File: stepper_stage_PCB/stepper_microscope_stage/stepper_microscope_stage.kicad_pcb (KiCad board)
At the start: 2 copper layers, 160.5 x 149.2 mm, 27 parts, among them J1 Conn_01x04_Socket, J2 Screw_Terminal_01x04, J3 Screw_Terminal_01x04, J4 Conn_01x04_Socket, J5 Conn_01x04_Socket, SW1 SW_SPDT

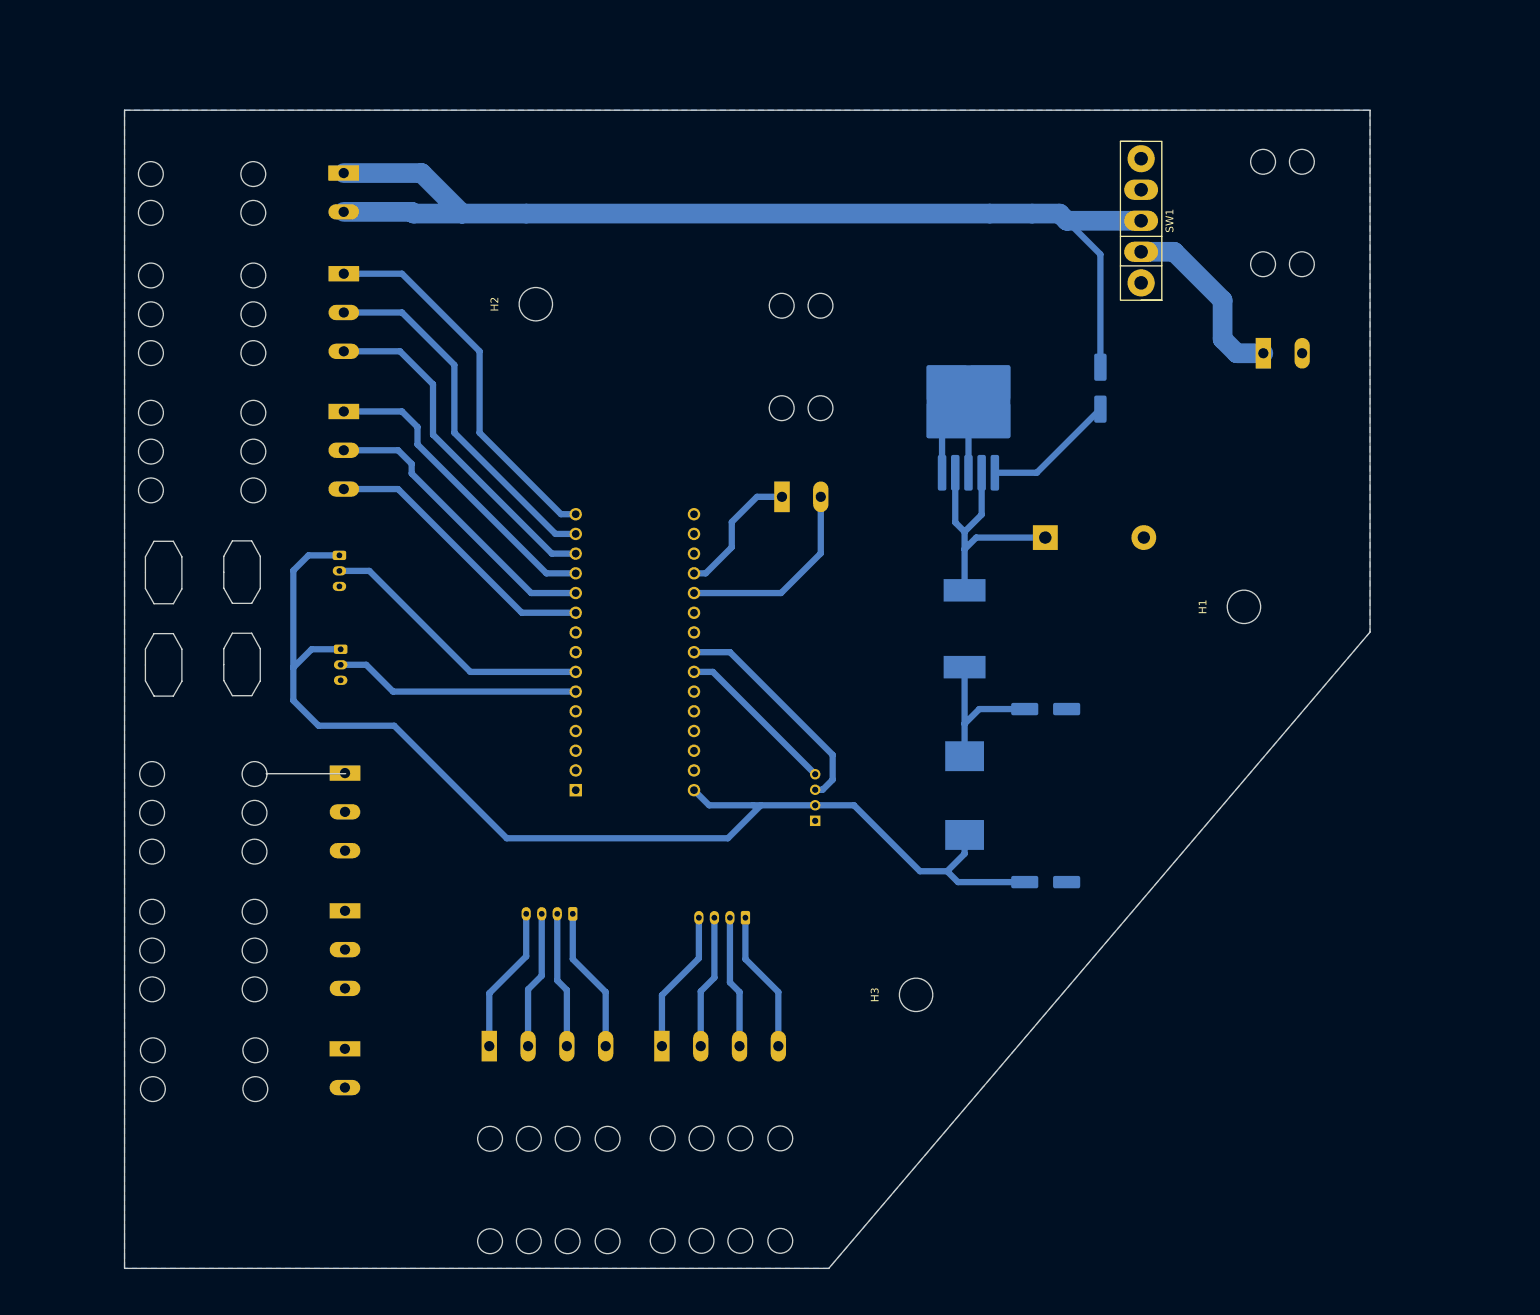
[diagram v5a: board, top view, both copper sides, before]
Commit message: Working. Must add following: (1) LCD space (2) ground plane
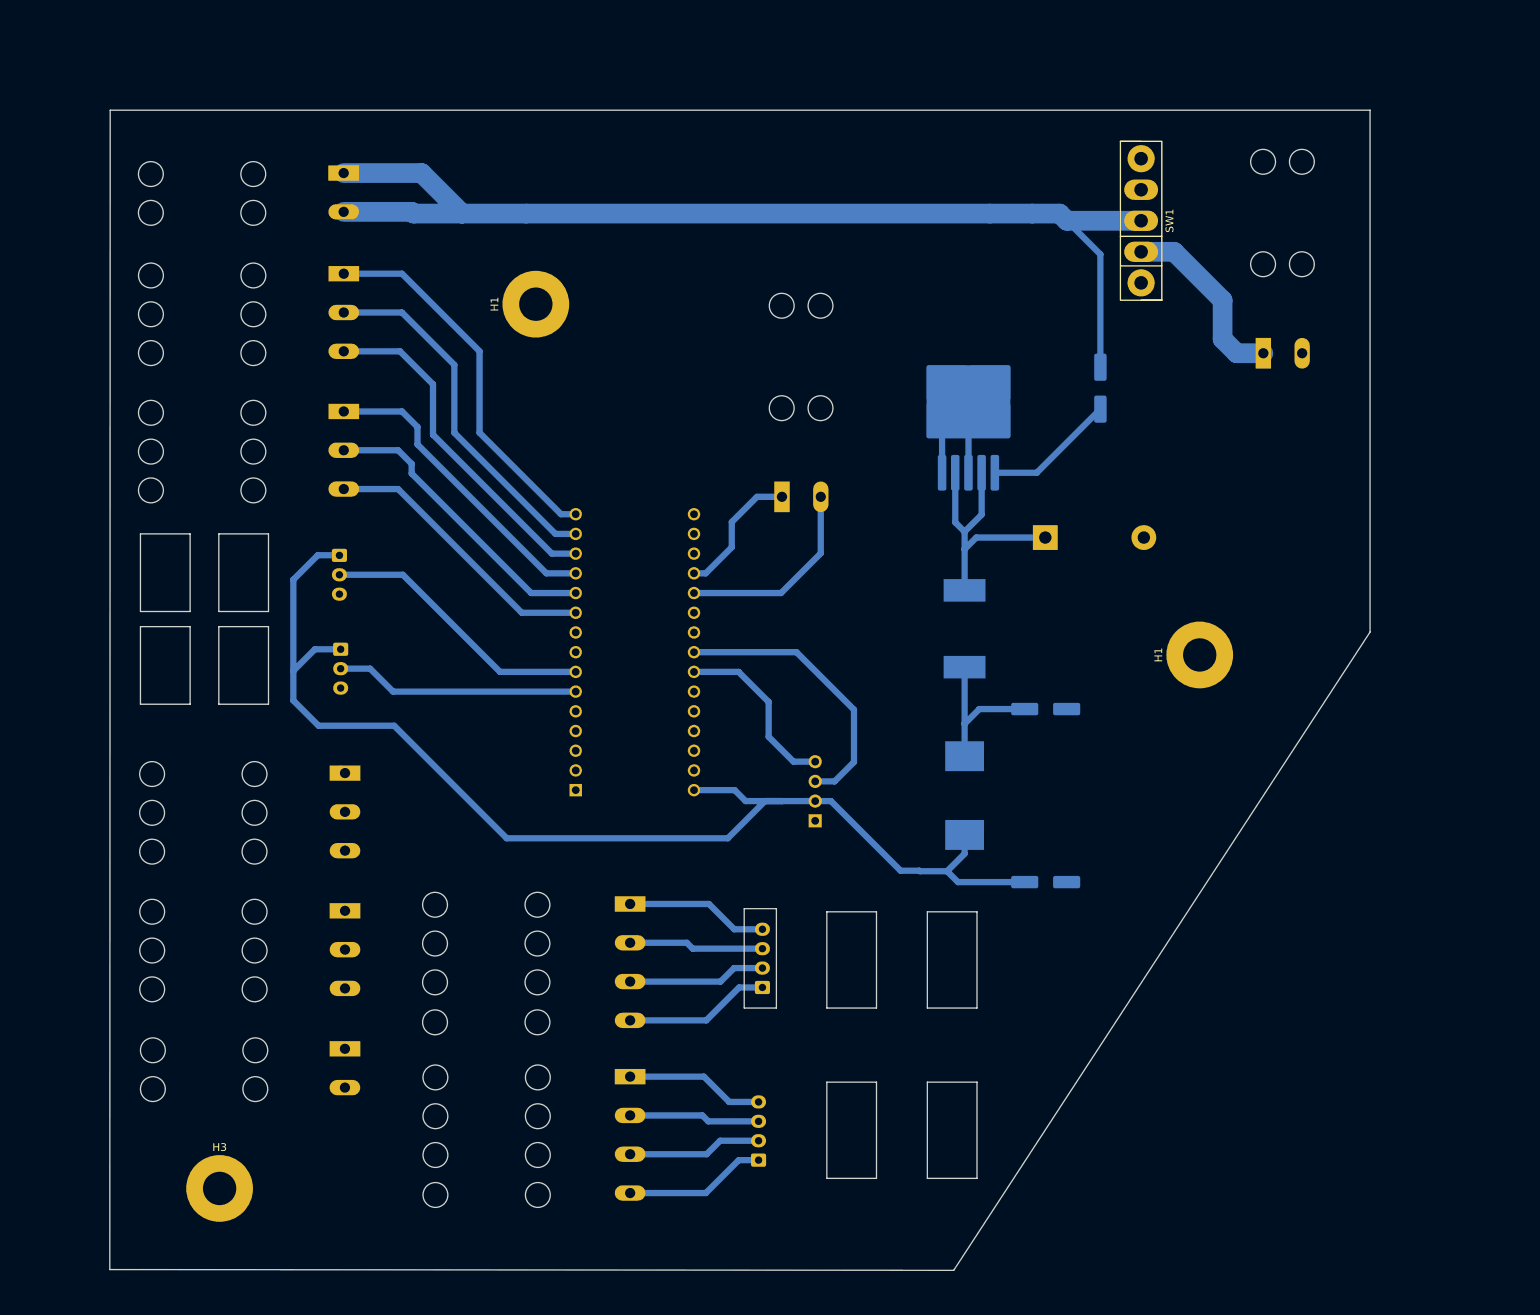
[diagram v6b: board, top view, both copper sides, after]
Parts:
- H1, H3: footprint MountingHole:MountingHole_4.3mm_M4 -> MountingHole:MountingHole_4.3mm_M4_Pad
- H1: renamed from H2; footprint MountingHole:MountingHole_4.3mm_M4 -> MountingHole:MountingHole_4.3mm_M4_Pad
- J1: footprint Connector_PinSocket_2.00mm:PinSocket_1x04_P2.00mm_Vertical -> Connector_PinSocket_2.54mm:PinSocket_1x04_P2.54mm_Vertical
- J4, J5: footprint Connector_JST:JST_PH_B4B-PH-K_1x04_P2.00mm_Vertical -> Connector_JST:JST_EH_B4B-EH-A_1x04_P2.50mm_Vertical
- LIMIT1, LIMIT2: footprint Connector_JST:JST_PH_B3B-PH-K_1x03_P2.00mm_Vertical -> Connector_JST:JST_EH_B3B-EH-A_1x03_P2.50mm_Vertical
- moved H3 93.2 mm to (53.8, 166.2), turned to 0 degrees
- moved J4 31.3 mm to (123.2, 162.6), turned to 90 degrees
- moved J5 26.2 mm to (123.7, 140.3), turned to 90 degrees
- moved J3 25.8 mm to (106.7, 129.5), turned to -90 degrees
- moved H1 8.42 mm to (180.1, 97.5)
- moved J2 5.68 mm to (106.7, 151.8), turned to -90 degrees
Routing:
- net Net-(A1-A4): track 29.3 -> 36.5 mm
- net +5V: track 153.1 -> 155.5 mm
- net Net-(A1-A5): track 21.1 -> 23.0 mm
- net +24V: track 168.4 -> 167.1 mm
- net Net-(J2-Pin_1): track 18.5 -> 17.9 mm
- net Net-(J3-Pin_1): track 19.0 -> 18.4 mm
- removed copper zone on B.Cu, net GND
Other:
- board size 160.5 x 149.2 mm -> 162.4 x 149.5 mm

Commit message: Large, but works
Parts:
- removed J1: Conn_01x04_Socket, Connector_PinSocket_2.54mm:PinSocket_1x04_P2.54mm_Vertical
- added J2: Conn_01x04_Socket, Connector_PinSocket_2.54mm:PinSocket_1x04_P2.54mm_Vertical, B.Cu at (151.7, 120.5)
- added REF**: Shop-style 16x2 LCD display, custom_LCDs:Shop-style 16x2 LCD display, B.Cu at (158.2, 103.2)
- moved H1 50.3 mm to (171.2, 147.0), turned to 180 degrees
- moved H1 43.2 mm to (53.8, 38.0), turned to 180 degrees
- moved C2 21.1 mm to (180.7, 99.3)
- moved C3 21.1 mm to (180.7, 121.6)
- moved C1 21.1 mm to (187.7, 58.0)
- moved SW1 21.1 mm to (192.9, 36.4)
- moved VIN1 21.1 mm to (208.7, 53.5)
- moved D1 21.1 mm to (180.6, 77.2)
- moved L1 21.1 mm to (170.2, 89.0)
- moved L2 21.1 mm to (170.2, 110.5)
- moved TL2575 21.1 mm to (170.7, 61.2)
- moved JOYIN1 18.3 mm to (114.8, 62.8)
- moved STEPPWR1 12.5 mm to (69.8, 22.8)
- moved LIMIT1 5.05 mm to (69.8, 89.6), turned to 90 degrees
- moved LIMIT2 0.31 mm to (69.2, 96.5)
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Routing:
- net +24V: track 167.1 -> 188.5 mm
- net Net-(A1-A5): track 23.0 -> 42.6 mm
- net +5V: track 155.5 -> 173.8 mm
- net Net-(A1-A4): track 36.5 -> 47.2 mm
- net Net-(A1-A0): track 17.3 -> 27.0 mm
- net Net-(A1-A1): track 25.7 -> 29.4 mm
- net Net-(A1-D4): track 35.6 -> 35.0 mm
- added copper zone on B.Cu, net GND
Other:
- board size 162.4 x 149.5 mm -> 182.2 x 161.7 mm

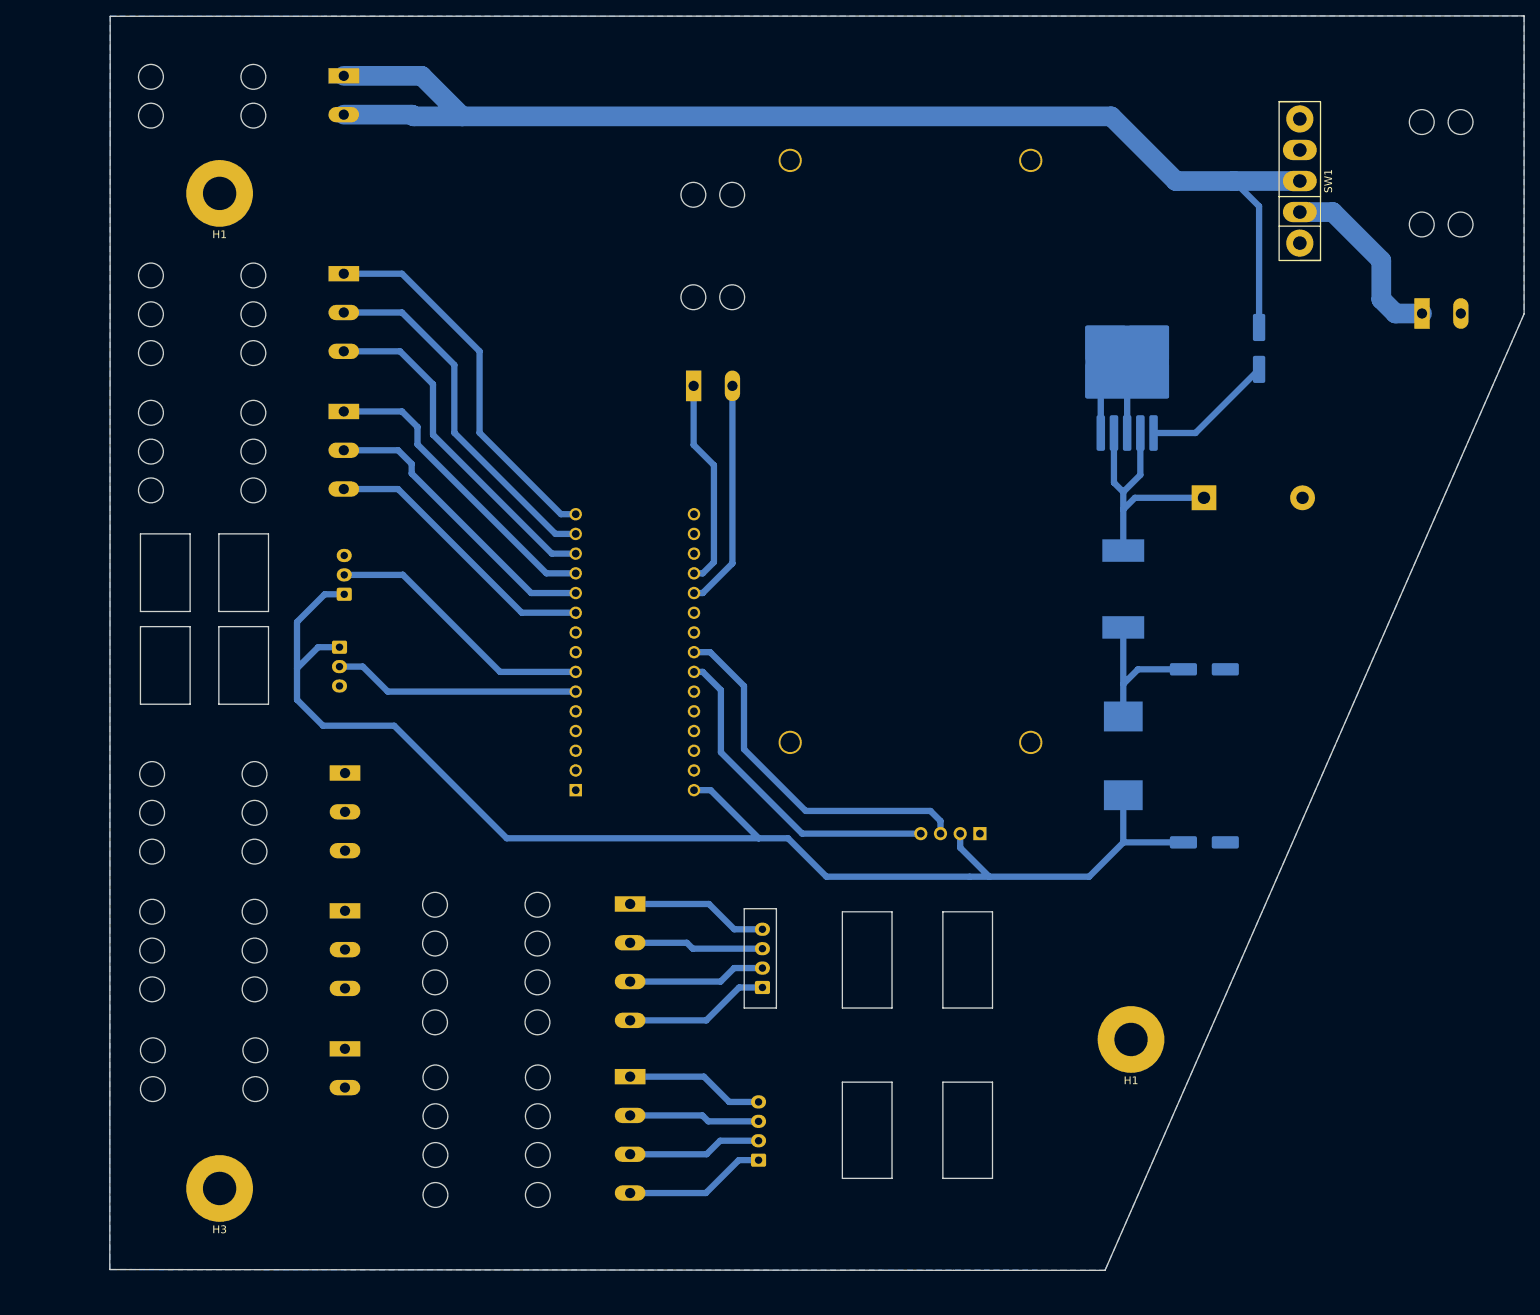
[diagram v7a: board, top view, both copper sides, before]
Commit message: Experimented with smaller PCB. Reorganized directories to be more clean
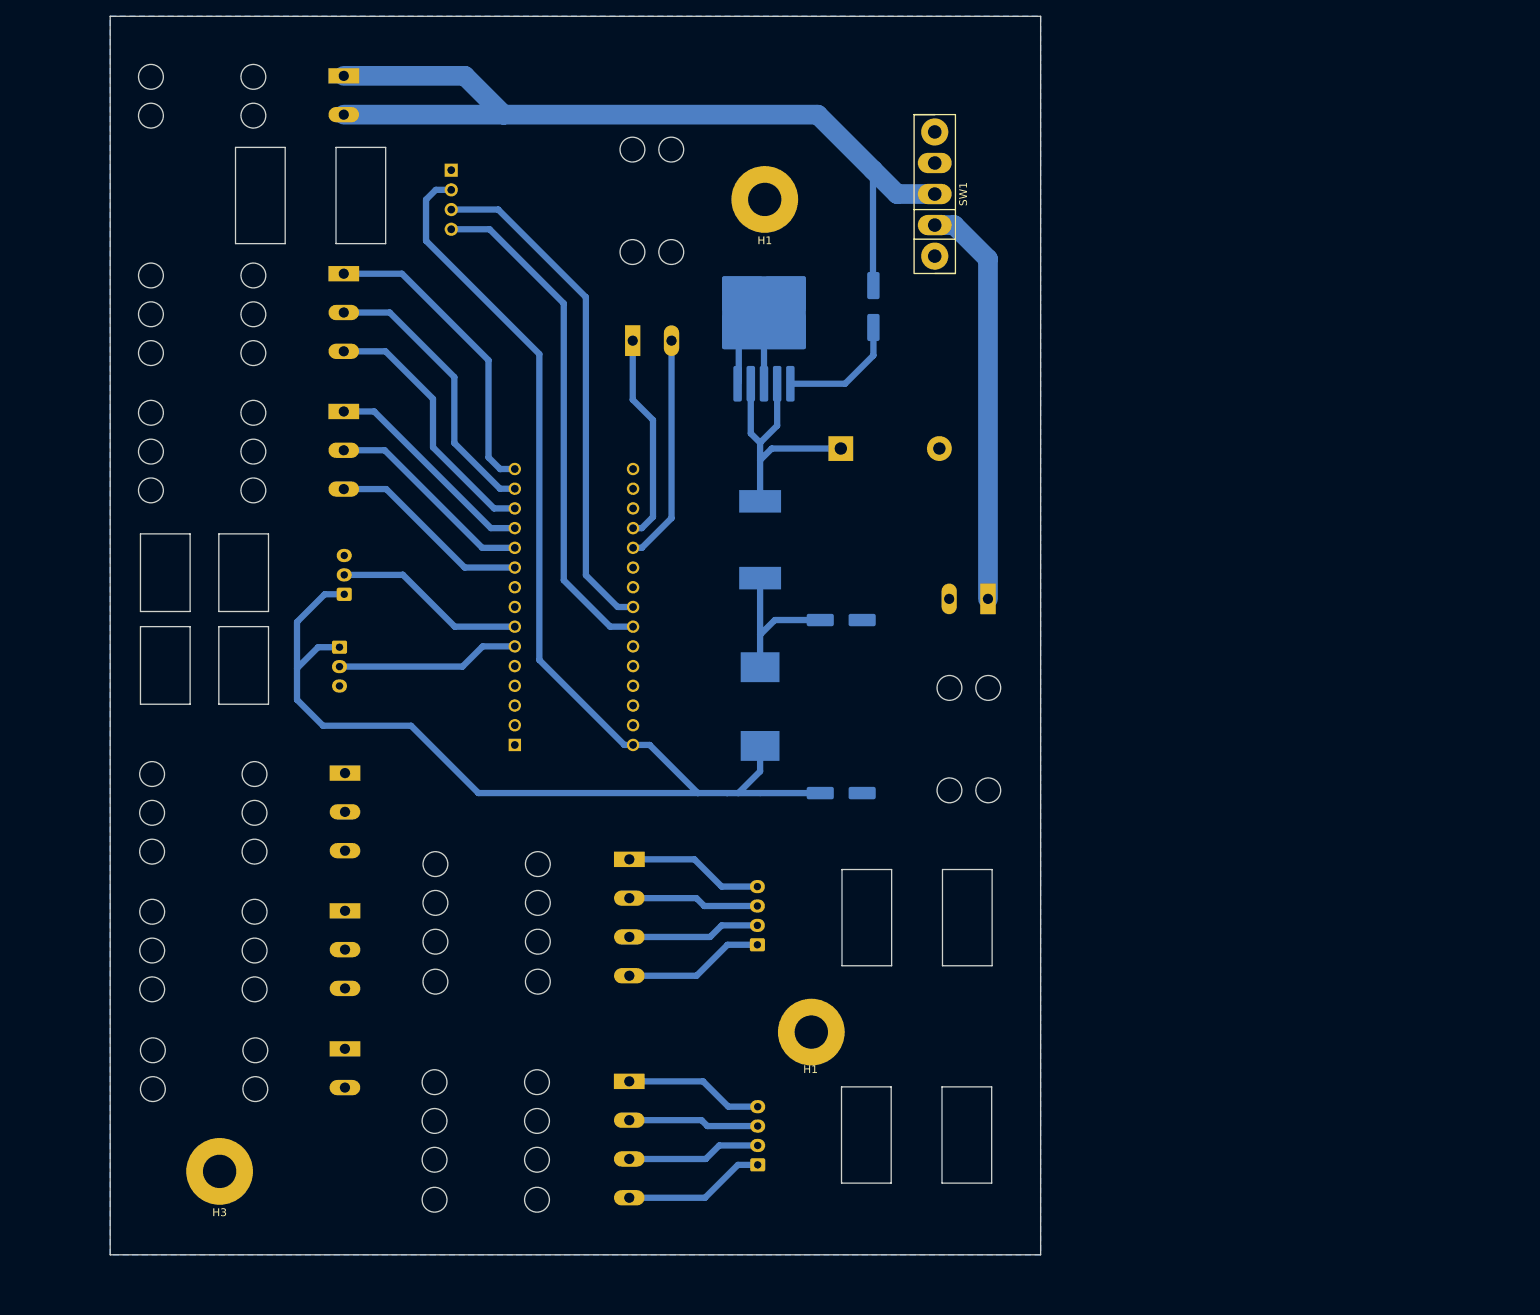
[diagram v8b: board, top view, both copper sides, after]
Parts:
- removed REF**: Shop-style 16x2 LCD display, custom_LCDs:Shop-style 16x2 LCD display
- moved H1 132.3 mm to (130.0, 146.1)
- moved H1 118.1 mm to (124.0, 38.8)
- moved J2 109.3 mm to (83.6, 35.0), turned to 180 degrees
- moved VIN1 66.9 mm to (152.8, 90.2), turned to 180 degrees
- moved C1 50.0 mm to (138.0, 52.5)
- moved C2 47.2 mm to (133.8, 93.0)
- moved C3 47.2 mm to (133.8, 115.2)
- moved D1 47.2 mm to (133.8, 70.8)
- moved L1 47.2 mm to (123.4, 82.6)
- moved L2 47.2 mm to (123.4, 104.1)
- moved TL2575 47.2 mm to (123.9, 54.9)
- moved SW1 47.1 mm to (145.9, 38.1)
- moved A1 9.78 mm to (91.8, 109.0)
- moved JOYIN1 9.78 mm to (107.0, 57.0)
- moved J3 5.75 mm to (106.5, 123.8)
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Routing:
- net +5V: track 173.8 -> 200.5 mm
- net Net-(A1-A5): track 42.6 -> 65.5 mm
- net Net-(A1-A4): track 47.2 -> 65.6 mm
- net +24V: track 188.5 -> 170.5 mm
- net Net-(A1-D9): track 39.8 -> 28.3 mm
- net Net-(A1-D8): track 38.2 -> 27.2 mm
- net Net-(A1-D10): track 44.5 -> 34.1 mm
- net Net-(A1-D11): track 46.8 -> 36.4 mm
- net Net-(A1-D7): track 36.5 -> 26.2 mm
- net Net-(A1-D4): track 35.0 -> 24.8 mm
- net Net-(A1-D12): track 48.9 -> 39.8 mm
- net Net-(A1-D3): track 31.8 -> 23.7 mm
- net Net-(TL2575-+Vin): track 17.0 -> 15.8 mm
- net Net-(J3-Pin_3): track 17.8 -> 17.1 mm
- net Net-(J3-Pin_4): track 18.8 -> 18.2 mm
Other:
- board size 182.2 x 161.7 mm -> 119.9 x 159.6 mm
